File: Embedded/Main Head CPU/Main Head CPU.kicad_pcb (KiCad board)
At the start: 4 copper layers, 50 x 47.5 mm, 53 parts, among them J1 10171746-00021LF, J10 Fan 1, J11 Substructure Power, J12 Head Power, J13 MicroSD, J14 Mic, J15 Expansion, J2 LEDs 0, J3 LEDs 1, J4 LEDs 2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

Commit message: Added Silkscreen Data
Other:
- board text added: "Designation: CSFB-Main-CPU Model No: CSF-AAA-001 Revision: D0.0"
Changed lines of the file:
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@@
 		(layer "F.SilkS")
+	)
+	(gr_rect
+		(start 93.75 71)
+		(end 106.25 74)
+		(stroke
+			(width 0.1)
+			(type default)
+		)
+		(fill no)
+		(layer "B.SilkS")
 	)
 	(gr_arc
@@
 		(layer "Edge.Cuts")
 	)
+	(gr_text "Designation: CSFB-Main-CPU\nModel No: CSF-AAA-001\nRevision: D0.0"
+		(at 106 72.5 0)
+		(layer "B.SilkS")
+		(effects
+			(font
+				(size 0.5 0.5)
+				(thickness 0.1)
+			)
+			(justify left mirror)
+		)
+	)
 	(segment

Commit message: Modified Asset Tags
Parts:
- moved G*** 0.25 mm to (99.8, 66.2)
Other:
- board text added: "Des: CSF-Main-CPU M/N: CSF-AAA-001 Rev: D0.0 Dat: 26.07.2025"
- board text removed: "Designation: CSFB-Main-CPU Model No: CSF-AAA-001 Revision: D0.0"
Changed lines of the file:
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@@
 	(footprint "LOGO"
 		(layer "B.Cu")
-		(at 99.75 66 180)
+		(at 99.75 66.25 180)
 		(property "Reference" "G***"
 			(at 0 0 0)
@@
 	)
 	(gr_rect
-		(start 93.75 71)
-		(end 106.25 74)
+		(start 95.75 70.25)
+		(end 104.25 73.75)
 		(stroke
 			(width 0.1)
@@
 		(layer "Edge.Cuts")
 	)
-	(gr_text "Designation: CSFB-Main-CPU\nModel No: CSF-AAA-001\nRevision: D0.0"
-		(at 106 72.5 0)
+	(gr_text "Des: CSF-Main-CPU\nM/N: CSF-AAA-001\nRev: D0.0\nDat: 26.07.2025"
+		(at 104 72 0)
 		(layer "B.SilkS")
 		(effects

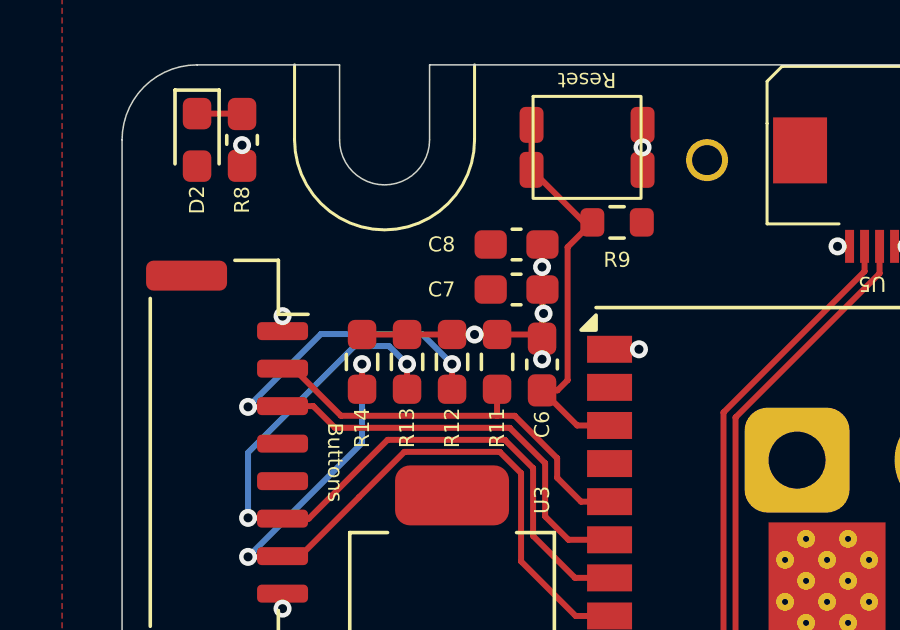
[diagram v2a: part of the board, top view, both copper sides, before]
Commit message: Modified Buttons from pull down to pull up
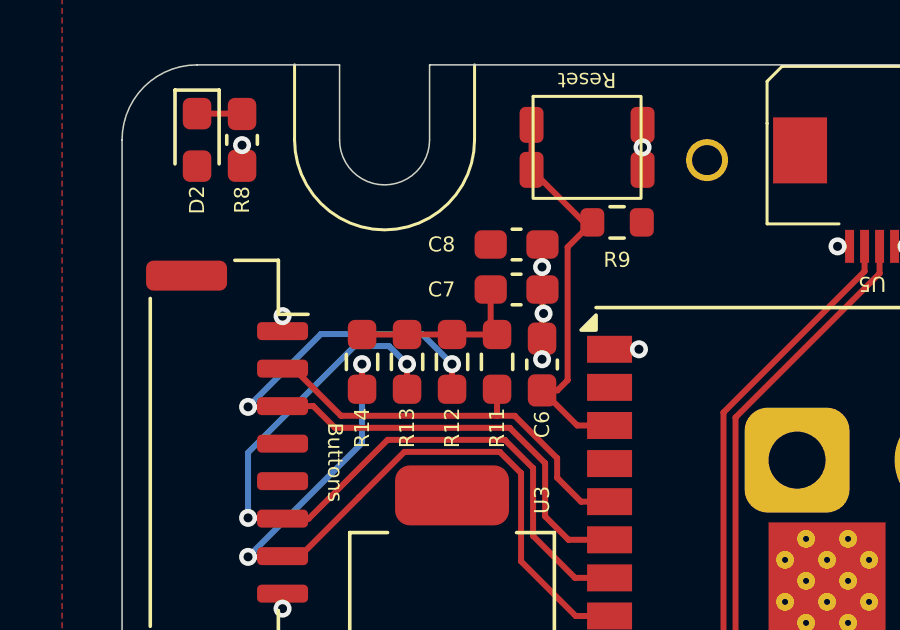
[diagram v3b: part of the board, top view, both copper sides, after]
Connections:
- R11 pad 1: GND -> +3V3
- R12 pad 1: GND -> +3V3
- R13 pad 1: GND -> +3V3
- R14 pad 1: GND -> +3V3
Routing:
- net GND: track 44.0 -> 37.4 mm, vias 60 -> 59
- net +3V3: track 0.00 -> 6.09 mm
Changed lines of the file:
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@@
 			(layers "F.Cu" "F.Mask" "F.Paste")
 			(roundrect_rratio 0.25)
-			(net 2 "GND")
+			(net 4 "+3V3")
 			(pintype "passive")
 		)
@@
 			(layers "F.Cu" "F.Mask" "F.Paste")
 			(roundrect_rratio 0.25)
-			(net 2 "GND")
+			(net 4 "+3V3")
 			(pintype "passive")
 		)
@@
 			(layers "F.Cu" "F.Mask" "F.Paste")
 			(roundrect_rratio 0.25)
-			(net 2 "GND")
+			(net 4 "+3V3")
 			(pintype "passive")
 		)
@@
 			(layers "F.Cu" "F.Mask" "F.Paste")
 			(roundrect_rratio 0.25)
-			(net 2 "GND")
+			(net 4 "+3V3")
 			(pintype "passive")
 		)
@@
 	)
 	(segment
-		(start 87.5 51.4875)
-		(end 86.75 51.4875)
-		(width 0.2)
-		(layer "F.Cu")
-		(net 2)
-	)
-	(segment
 		(start 88.8625 51.4875)
 		(end 89 51.625)
@@
 	)
 	(segment
-		(start 83 51.4875)
-		(end 86.75 51.4875)
-		(width 0.2)
-		(layer "F.Cu")
-		(net 2)
-	)
-	(segment
 		(start 114.0875 69.5)
 		(end 114.924313 69.5)
@@
 	)
 	(segment
-		(start 86.75 51.4875)
-		(end 88.8625 51.4875)
-		(width 0.2)
-		(layer "F.Cu")
-		(net 2)
-	)
-	(segment
 		(start 89 51.625)
 		(end 89 52.3125)
@@
 	)
 	(via
-		(at 86.75 51.4875)
-		(size 0.6)
-		(drill 0.3)
-		(layers "F.Cu" "B.Cu")
-		(net 2)
-	)
-	(via
 		(at 111.7 63.15)
 		(size 0.6)
@@
 	)
 	(segment
+		(start 87.2875 49.9875)
+		(end 87.2875 51.275)
+		(width 0.2)
+		(layer "F.Cu")
+		(net 4)
+	)
+	(segment
+		(start 83 51.4875)
+		(end 87.5 51.4875)
+		(width 0.2)
+		(layer "F.Cu")
+		(net 4)
+	)
+	(segment
+		(start 87.2875 51.275)
+		(end 87.5 51.4875)
+		(width 0.2)
+		(layer "F.Cu")
+		(net 4)
+	)
+	(segment
